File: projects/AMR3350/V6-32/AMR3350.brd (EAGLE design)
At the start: 162 x 87 mm, 241 parts, among them IC1 LDO-TS1117CW-3V3, IC10 TMC21X0-LA, IC11 74LS32D, IC2 ATSAM4S8C, IC3 SI87XXIS, IC4 74HC125, IC5 74S08D, IC6 TMC21X0-LA, IC7 TMC21X0-LA, IC8 TMC21X0-LA, IC9 TMC21X0-LA, J1 MOLEX-105162-001, J2 MSTBV4, Q1 NX138BKS, Q2 NX138BKS, Q3 BUK9Y53-100B, Q4 BUK9Y53-100B, U1 A4403, X1 USB-B_TH, X2 12MHz, X3 KK-254-2, X4 KK-254-4, X5 KK-254-4, X6 KK-254-4, X7 KK-254-4, X8 KK-254-4, X9 KK-254-4

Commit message: Progress
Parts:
- moved R55 37.3 mm to (107.2, 61.7)
- moved IC8 35.1 mm to (81.3, 62.6), turned to 90 degrees
- moved C104 5.08 mm to (34.3, 76.2)
- moved X8 5.08 mm to (43.2, 76.2)
- moved X7 3.81 mm to (62.2, 76.2)
- moved C91 3.81 mm to (53.3, 76.2)
- moved C78 2.54 mm to (72.4, 76.2)
- moved X6 2.54 mm to (81.3, 83.2)
- moved X9 2.54 mm to (81.3, 76.2)
- moved C65 1.27 mm to (91.4, 76.2)
- moved IC7 1.27 mm to (100.3, 62.6)
- moved X5 1.27 mm to (100.3, 76.2)
- turned IC10 to 90 degrees
- turned IC9 to 90 degrees
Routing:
- net +12V: track 14.6 -> 73.0 mm
- net A1_Z: track 0.00 -> 35.9 mm, vias 0 -> 3
- net B1_Z: track 0.00 -> 33.0 mm, vias 0 -> 3
- net GND: track 7.28 -> 36.4 mm, vias 12 -> 60
- net A1_X2: track 28.9 -> 0.00 mm, vias 3 -> 0
- net A1_X1: track 28.9 -> 0.00 mm, vias 3 -> 0
- net A1_X3: track 28.9 -> 0.00 mm, vias 3 -> 0
- net A1_X4: track 28.9 -> 0.00 mm, vias 3 -> 0
- net A1_E2: track 0.00 -> 28.9 mm, vias 0 -> 3
- net A1_E1: track 0.00 -> 28.9 mm, vias 0 -> 3
- net A1_Y: track 0.00 -> 28.9 mm, vias 0 -> 3
- net ENN: track 7.11 -> 35.6 mm, vias 1 -> 5
- net B2_Z: track 0.00 -> 28.3 mm, vias 0 -> 3
- net A2_Z: track 0.00 -> 27.7 mm, vias 0 -> 3
- net B1_X3: track 26.1 -> 0.00 mm, vias 3 -> 0
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- added copper zone on layer 1, net A1_E1
- added copper zone on layer 16, net A1_E1
- added copper zone on layer 1, net A1_E2
- added copper zone on layer 16, net A1_E2
- added copper zone on layer 1, net A1_Y
- added copper zone on layer 16, net A1_Y
- added copper zone on layer 1, net A1_Z
- added copper zone on layer 16, net A1_Z
- added copper zone on layer 1, net A2_E1
- added copper zone on layer 16, net A2_E1
- added copper zone on layer 1, net A2_E2
- added copper zone on layer 16, net A2_E2
- added copper zone on layer 1, net A2_Y
- added copper zone on layer 16, net A2_Y
- added copper zone on layer 1, net A2_Z
- added copper zone on layer 16, net A2_Z
- added copper zone on layer 1, net B1_E1
- added copper zone on layer 16, net B1_E1
- added copper zone on layer 1, net B1_E2
- added copper zone on layer 16, net B1_E2
- added copper zone on layer 1, net B1_Y
- added copper zone on layer 16, net B1_Y
- added copper zone on layer 1, net B1_Z
- added copper zone on layer 16, net B1_Z
- added copper zone on layer 1, net B2_E1
- added copper zone on layer 16, net B2_E1
- added copper zone on layer 1, net B2_E2
- added copper zone on layer 16, net B2_E2
- added copper zone on layer 1, net B2_Z
- added copper zone on layer 16, net B2_Z
- removed copper zone on layer 1, net A1_X1
- removed copper zone on layer 16, net A1_X1
- removed copper zone on layer 1, net A1_X2
- removed copper zone on layer 16, net A1_X2
- removed copper zone on layer 1, net A1_X3
- removed copper zone on layer 16, net A1_X3
- removed copper zone on layer 1, net A1_X4
- removed copper zone on layer 16, net A1_X4
- removed copper zone on layer 1, net A2_X1
- removed copper zone on layer 16, net A2_X1
- removed copper zone on layer 1, net A2_X2
- removed copper zone on layer 16, net A2_X2
- removed copper zone on layer 1, net A2_X3
- removed copper zone on layer 16, net A2_X3
- removed copper zone on layer 1, net A2_X4
- removed copper zone on layer 16, net A2_X4
- removed copper zone on layer 1, net B1_X1
- removed copper zone on layer 16, net B1_X1
- removed copper zone on layer 1, net B1_X2
- removed copper zone on layer 16, net B1_X2
- removed copper zone on layer 1, net B1_X3
- removed copper zone on layer 16, net B1_X3
- removed copper zone on layer 1, net B1_X4
- removed copper zone on layer 16, net B1_X4
- removed copper zone on layer 1, net B2_X2
- removed copper zone on layer 16, net B2_X2
- removed copper zone on layer 1, net B2_X3
- removed copper zone on layer 16, net B2_X3
- removed copper zone on layer 1, net B2_X4
- removed copper zone on layer 16, net B2_X4

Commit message: More progress
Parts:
- moved C71 220.0 mm to (103.8, 72.1), turned to 180 degrees
- moved C70 211.9 mm to (102.0, 71.0)
- moved C69 202.2 mm to (98.7, 71.0), turned to 180 degrees
- moved C81 200.4 mm to (77.9, 72.1)
- moved C68 194.1 mm to (96.9, 72.1)
- moved C107 164.6 mm to (39.8, 72.1)
- moved C97 125.0 mm to (65.7, 72.1), turned to 180 degrees
- moved C84 118.7 mm to (84.7, 72.1), turned to 180 degrees
- moved C96 117.0 mm to (63.9, 71.0)
- moved C83 110.7 mm to (82.9, 71.0)
- moved C95 107.4 mm to (60.6, 71.0), turned to 180 degrees
- moved C82 101.0 mm to (79.6, 71.0), turned to 180 degrees
- moved C94 99.2 mm to (58.8, 72.1)
- moved C109 72.9 mm to (44.8, 71.0)
- moved C110 67.9 mm to (46.6, 72.1), turned to 180 degrees
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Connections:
- net FAN1_D1 renamed FAN3_D
- net FAN1_G1 renamed FAN3_G
- net FAN2_D1 renamed FAN4_D
- net FAN2_G1 renamed FAN4_G
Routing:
- net IREF_X4: track 4.30 -> 0.00 mm
- net IREF_E2: track 0.00 -> 4.30 mm
- net BRB_X3: track 2.81 -> 0.00 mm
- net BRB_E1: track 0.00 -> 2.81 mm
- net BRB_X4: track 2.81 -> 0.00 mm
- net BRB_E2: track 0.00 -> 2.81 mm
- net BRA_X3: track 2.80 -> 0.00 mm
- net BRA_E1: track 0.00 -> 2.80 mm
- removed copper zone on layer 1, net B2_E2

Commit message: Some traces
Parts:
- added F2, F3: (no value), fuse:19560
- moved Y_STOP 232.4 mm to (114.3, 69.8)
- moved IC3 223.8 mm to (108.3, 83.7), turned to 90 degrees
- moved X_STOP 218.4 mm to (114.3, 62.9)
- moved C23 207.4 mm to (81.7, 34.5), turned to 270 degrees
- moved C17 194.9 mm to (77.1, 45.8), turned to 90 degrees
- moved C63 192.9 mm to (76.7, 67.8), turned to 270 degrees
- moved C67 191.3 mm to (87.8, 66.2)
- moved R57 188.9 mm to (81.8, 70.5), turned to 180 degrees
- moved C72 187.4 mm to (64.8, 60.1)
- moved C66 184.5 mm to (74.7, 67.8), turned to 90 degrees
- moved X2 182.0 mm to (74.5, 24.6), turned to 270 degrees
- moved R61 180.1 mm to (62.7, 70.5), turned to 180 degrees
- moved R56 177.8 mm to (85.0, 69.2), turned to 180 degrees
- moved C20 174.6 mm to (71.8, 26.4), turned to 90 degrees
- moved C21 174.1 mm to (77.5, 25.7), turned to 90 degrees
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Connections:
- net EXT_D renamed EXT1_D
- net EXT_G renamed EXT1_G
- removed net ADVREF1: C24.1, IC2.1, L4.1
- new net N$1: F2.2, J2.2
- new net N$2: F3.2, J2.4
- new net N$3: X6.1, X9.2
- new net N$4: X6.4, X9.3
- net +12V: now also F2.1, F3.1; no longer J2.2, J2.4
- net A1_Z: no longer X6.1
- net A2_Z: no longer X9.2
- net ADVREF: now also C24.1, IC2.1, L4.1
- net B1_Z: no longer X9.3
- net B2_Z: no longer X6.4
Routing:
- net +12V: track 73.0 -> 470.8 mm
- net GND: track 36.4 -> 402.6 mm, vias 60 -> 124
- net X_STEP: track 0.00 -> 34.8 mm
- net X_DIR: track 0.00 -> 34.8 mm
- net X_EN: track 0.00 -> 34.2 mm
- net E1_DIR: track 0.00 -> 26.9 mm
- net USB_N: track 31.0 -> 7.39 mm
- net USB_P: track 31.1 -> 7.42 mm
- net A2_Z: track 27.7 -> 4.28 mm
- net Y_EN: track 0.00 -> 22.6 mm
- net Y_STEP: track 0.00 -> 22.1 mm
- net Y_DIR: track 0.00 -> 22.1 mm
- net EXT1_D: track 0.00 -> 21.2 mm, vias 0 -> 23
- net EXT2_D: track 0.00 -> 21.2 mm, vias 0 -> 23
- net Z_DIR: track 0.00 -> 19.6 mm
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- added copper zone on layer 1, net B2_E2
- added copper zone on layer 1, net EXT1_D
- added copper zone on layer 16, net EXT1_D
- added copper zone on layer 1, net EXT2_D
- added copper zone on layer 16, net EXT2_D
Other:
- board size 162 x 87 mm -> 118.8 x 87 mm

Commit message: Almost done*
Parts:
- D1: device diode:SMC -> diode:SMB
- moved R14 165.7 mm to (95.2, -24.1)
- moved R39 158.0 mm to (106.0, -16.6)
- moved C41 150.1 mm to (109.2, -21.6)
- moved C42 150.1 mm to (104.1, -21.6)
- moved C43 150.1 mm to (99.1, -21.6)
- moved R36 150.1 mm to (113.0, -9.53)
- moved R37 150.1 mm to (108.0, -9.53)
- moved R38 150.1 mm to (110.5, -14.6)
- moved R41 150.1 mm to (106.0, -14.6)
- moved R40 147.6 mm to (106.0, -18.7)
- moved BED 117.7 mm to (96.5, 3.56)
- moved EXT1 117.7 mm to (90.8, 3.56)
- moved EXT2 117.7 mm to (85.1, 3.56)
- moved L6 111.8 mm to (81.0, 49.9), turned to 180 degrees
- moved C45 103.7 mm to (83.9, 28.7), turned to 270 degrees
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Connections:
- removed net N$6: IC11.10, IC11.3
- new net ESP_RST: ESP1.1, R18.2, R22.2
- new net N$5: IC11.10, IC11.6
- net ESP_RESET: no longer ESP1.1, R18.2, R22.2
- net GND: now also IC5.10, IC5.9; no longer IC5.1, IC5.2
- net LCD_CS: now also IC5.2; no longer IC5.10
- net LCD_ENC_A: now also IC2.83; no longer IC2.82
- net LCD_ENC_B: now also IC2.82; no longer IC2.83
- net LCD_MOSI: now also IC5.1; no longer IC5.9
- net LCD_MOSI_BUF: now also IC5.3; no longer IC5.8
- net N$7: now also IC11.3; no longer IC11.6
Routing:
- net ENN: track 33.7 -> 207.9 mm, vias 4 -> 11
- net MOT_MOSI: track 0.00 -> 128.5 mm, vias 0 -> 5
- net MOT_SCK: track 0.00 -> 125.0 mm, vias 0 -> 5
- net MOT_MISO: track 0.00 -> 102.8 mm, vias 0 -> 5
- net +3V3: track 26.6 -> 113.1 mm, vias 0 -> 14
- net SG_TST_X: track 6.65 -> 79.7 mm, vias 1 -> 4
- net LCD_SCK: track 0.00 -> 62.0 mm, vias 0 -> 4
- net LCD_MISO: track 0.00 -> 59.2 mm, vias 0 -> 2
- net LCD_MOSI: track 0.00 -> 58.3 mm, vias 0 -> 2
- net SG_TST_E2: track 6.65 -> 64.1 mm, vias 1 -> 2
- net SG_TST_Y: track 6.65 -> 61.9 mm, vias 1 -> 4
- net E2_EN: track 0.00 -> 55.0 mm
- net MCDA2: track 0.00 -> 54.5 mm, vias 0 -> 2
- net VDDOUT: track 6.64 -> 59.9 mm, vias 0 -> 5
- net E2_STEP: track 0.00 -> 52.3 mm
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- added copper zone on layer 1, net +3V3
- added copper zone on layer 16, net +3V3
- added copper zone on layer 1, net +5V
- added copper zone on layer 1, net GND
- added copper zone on layer 16, net GND
- added copper zone on layer 1, net LX
- added copper zone on layer 1, net VOUT
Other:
- board size 118.8 x 87 mm -> 100 x 87 mm

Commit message: Almost** done*
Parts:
- moved Z_STOP 89.0 mm to (24.1, 47.6), turned to 90 degrees
- moved IC3 84.3 mm to (43.9, 28.6), turned to 270 degrees
- moved Y_STOP 80.2 mm to (31.1, 47.6), turned to 90 degrees
- moved SJ2 76.7 mm to (24.1, 52.1)
- moved R49 72.8 mm to (32.0, 33.1)
- moved SJ1 72.3 mm to (27.9, 52.1), turned to 180 degrees
- moved R48 72.1 mm to (32.0, 31.1)
- moved X_STOP 71.6 mm to (38.1, 47.6), turned to 90 degrees
- moved R14 65.2 mm to (77.9, 38.7), turned to 270 degrees
- moved C43 61.4 mm to (78.4, 36.2)
- moved C41 60.8 mm to (79.9, 31.6), turned to 90 degrees
- moved EXT1_L 58.7 mm to (28.6, 31.1), turned to 90 degrees
- moved EXT2_L 56.3 mm to (28.6, 33.1), turned to 90 degrees
- moved R36 56.1 mm to (77.9, 34.2)
- moved R38 55.7 mm to (77.3, 30.1)
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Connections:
- net BED: now also IC2.86; no longer IC2.25
- net ESP_DATA_RDY: now also IC2.13; no longer IC2.40
- net FAN_E1: now also IC2.40; no longer IC2.93
- net FAN_E2: now also IC2.25; no longer IC2.86
- net PWR_FAIL_DET2: now also IC2.6; no longer IC2.23
- net X_STOP: now also IC2.73
- net Y_STOP: now also IC2.74
- net Z_STOP: now also IC2.75
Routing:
- net GND: track 453.5 -> 1347.7 mm, vias 139 -> 208
- net +3V3: track 113.1 -> 365.9 mm, vias 14 -> 26
- net +5V: track 33.5 -> 189.3 mm, vias 0 -> 2
- net FAN_E2: track 0.00 -> 70.1 mm, vias 0 -> 2
- net FAN_MOBO: track 0.00 -> 69.9 mm, vias 0 -> 2
- net FAN_PART: track 0.00 -> 68.1 mm, vias 0 -> 2
- net EXT1: track 0.00 -> 66.1 mm, vias 0 -> 2
- net PWR_FAIL_DET2: track 0.00 -> 64.9 mm, vias 0 -> 2
- net EXT2: track 0.00 -> 60.7 mm, vias 0 -> 2
- net VSSA: track 0.00 -> 60.1 mm, vias 0 -> 1
- net BED: track 0.00 -> 57.1 mm
- net FAN_E1: track 0.00 -> 49.3 mm, vias 0 -> 4
- net +12V: track 476.8 -> 521.8 mm, vias 0 -> 1
- net T_BED_IN: track 0.00 -> 44.3 mm, vias 0 -> 2
- net MOT_MISO: track 102.8 -> 136.1 mm, vias 5 -> 7
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
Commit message: Done***
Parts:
- moved C22 86.3 mm to (77.3, 41.3), turned to 180 degrees
- moved 5V 64.7 mm to (54.9, 18.4), turned to 270 degrees
- moved R9 59.7 mm to (58.4, 18.4)
- moved R10 59.1 mm to (58.4, 20.4)
- moved VIN 58.3 mm to (54.9, 14.4), turned to 270 degrees
- moved R11 58.0 mm to (58.4, 16.4)
- moved USB 57.3 mm to (54.9, 16.4), turned to 270 degrees
- moved R8 53.3 mm to (58.4, 14.4)
- moved 3V1 49.9 mm to (54.9, 20.4), turned to 270 degrees
- moved R16 44.8 mm to (35.8, 35.4), turned to 90 degrees
- moved C35 44.5 mm to (35.8, 32.4), turned to 270 degrees
- moved C14 11.1 mm to (51.6, 22.2)
- moved C86 0.89 mm to (28.3, 70.7)
- moved C99 0.89 mm to (9.27, 70.7)
- moved C73 0.89 mm to (47.4, 70.7)
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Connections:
- net RESET: now also RESET.A'; no longer RESET.A
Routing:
- net +5V: track 189.3 -> 378.7 mm, vias 2 -> 13
- net GND: track 1347.7 -> 1443.3 mm, vias 208 -> 223
- net +12V: track 521.8 -> 591.6 mm, vias 1 -> 2
- net +3V3: track 365.9 -> 394.3 mm, vias 26 -> 27
- net RESET: track 0.00 -> 28.2 mm, vias 0 -> 2
- net VBUS: track 11.7 -> 31.0 mm
- net VSSA: track 60.1 -> 64.4 mm
- net USB_LED: track 0.00 -> 1.66 mm
- net 5V_LED: track 0.00 -> 1.66 mm
- net 3V3_LED: track 0.00 -> 1.66 mm
- net 24V_LED: track 0.00 -> 1.66 mm
- net MCDA0: track 39.6 -> 41.0 mm
- net MCCK: track 37.7 -> 39.2 mm
- net MCDA1: track 36.0 -> 37.5 mm
- net E2_STEP: track 54.3 -> 55.2 mm
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
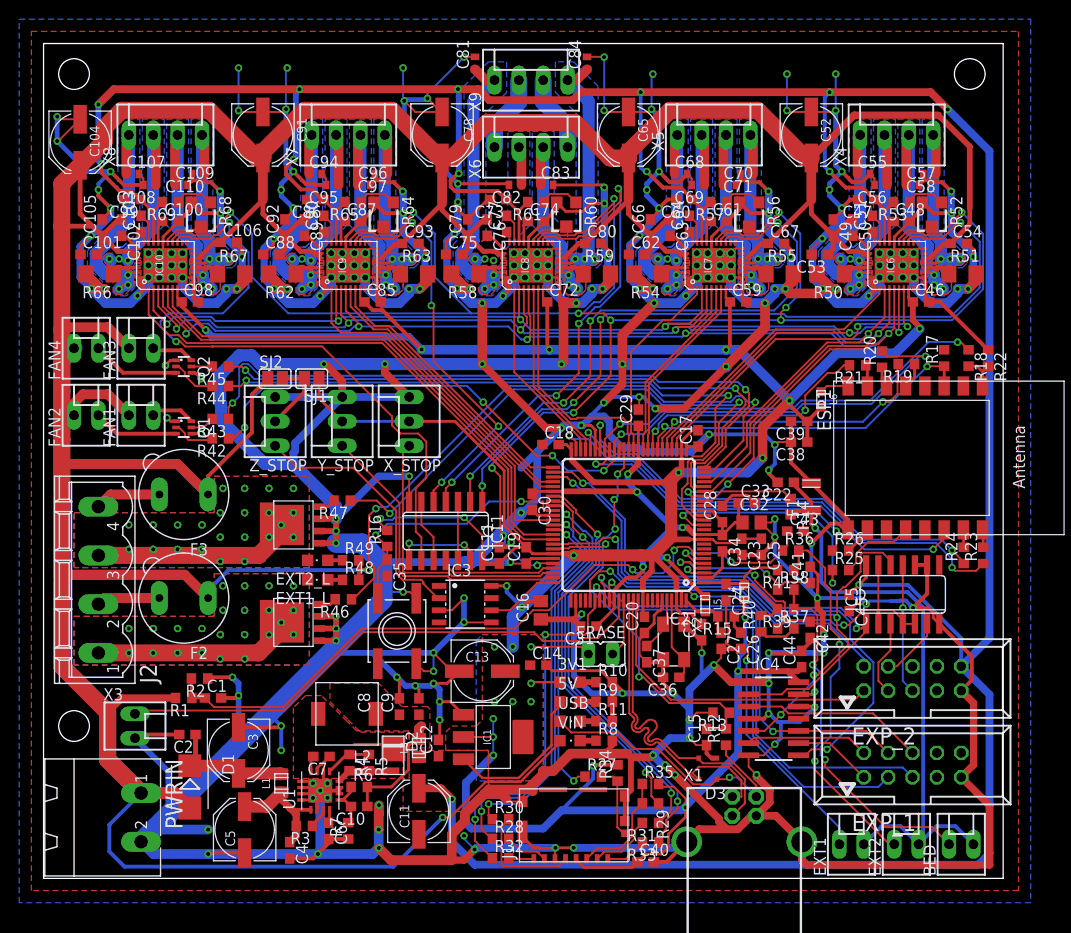
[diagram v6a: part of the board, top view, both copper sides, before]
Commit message: Added a resistor
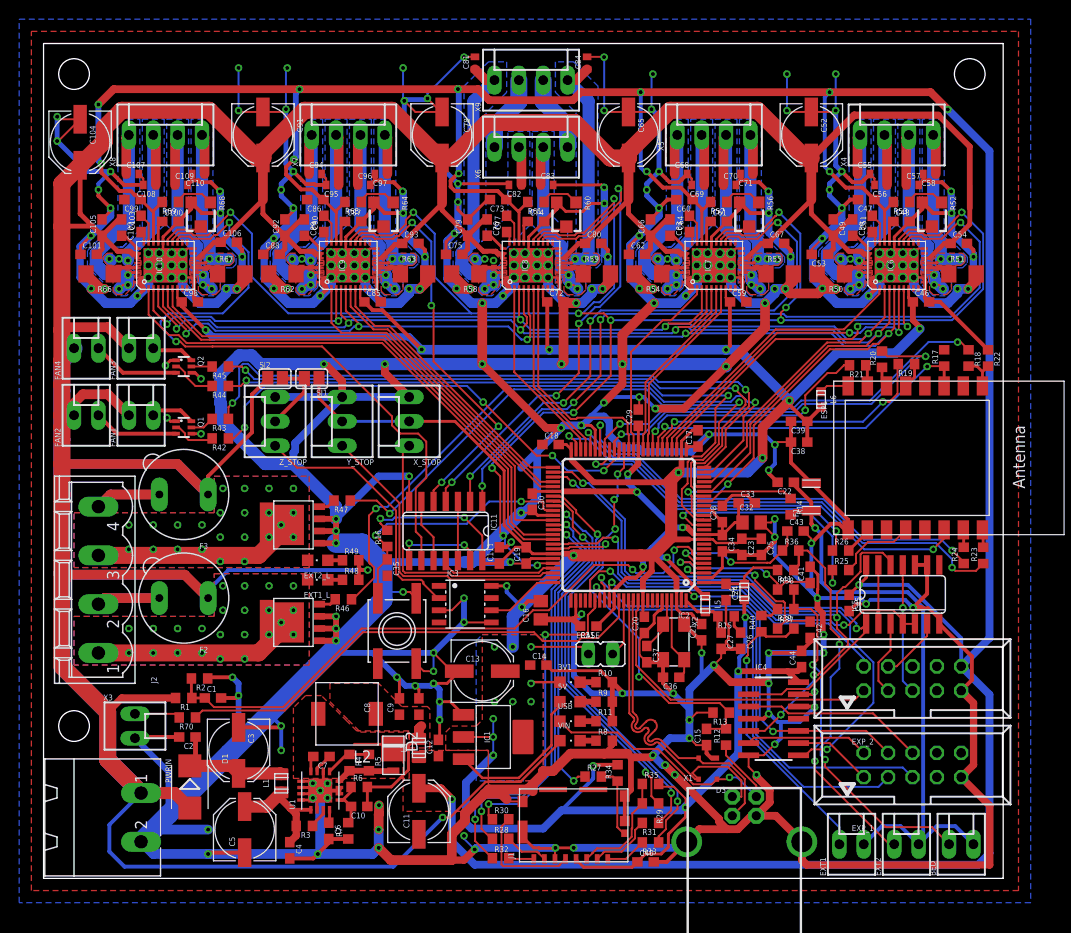
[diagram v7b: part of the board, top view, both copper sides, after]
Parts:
- added R70: 180R, resistor:R0603
- moved C2 0.25 mm to (15.0, 14.7)
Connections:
- new net BED_OUT: R70.2, X3.1
- net BED: now also R70.1; no longer X3.1
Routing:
- net BED: track 57.1 -> 50.9 mm
- net BED_OUT: track 0.00 -> 4.77 mm
